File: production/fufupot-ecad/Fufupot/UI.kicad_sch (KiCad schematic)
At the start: 4 parts

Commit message: Updates unfinished
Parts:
- removed BZ1: Buzzer, symbol Device:Buzzer
- removed D1: LED, symbol Device:LED
- removed R1: 220, symbol Device:R
- removed R2: 330, symbol Device:R

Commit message: UI without button
UI schematic without the button
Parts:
- added BZ1: Buzzer, symbol Device:Buzzer
- added D1: LED, symbol Device:LED
- added R1: 220, symbol Device:R
- added R2: 330, symbol Device:R
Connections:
- new net: D1.1 (K), R1.2
- new net D1: BZ1.1 (-)
- new net D2: R1.1
- new net D3: R2.1
- new net GND: BZ1.2 (+), D1.2 (A)
- new net LED_SGN: R2.2

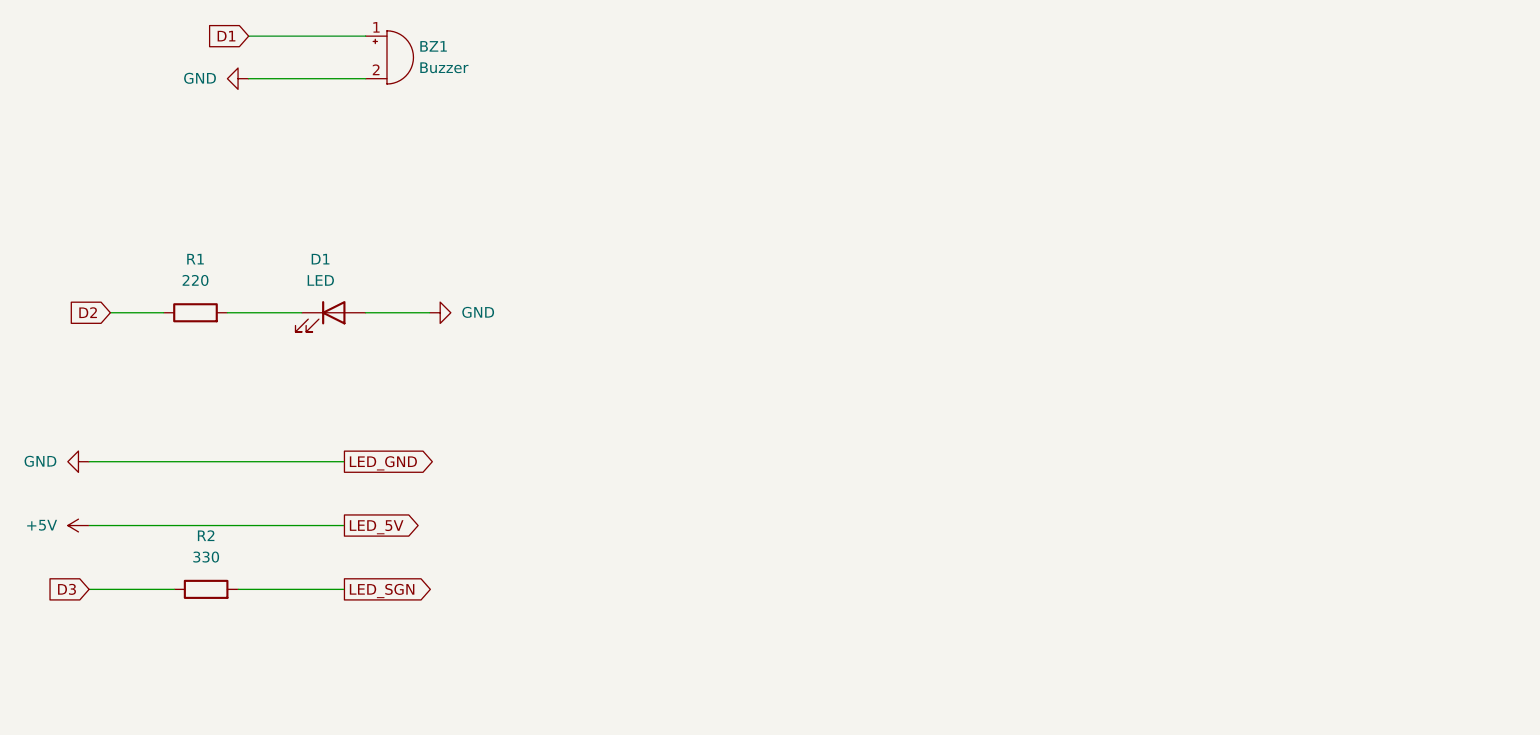
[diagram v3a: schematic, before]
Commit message: UI with Button
Added the button circuit
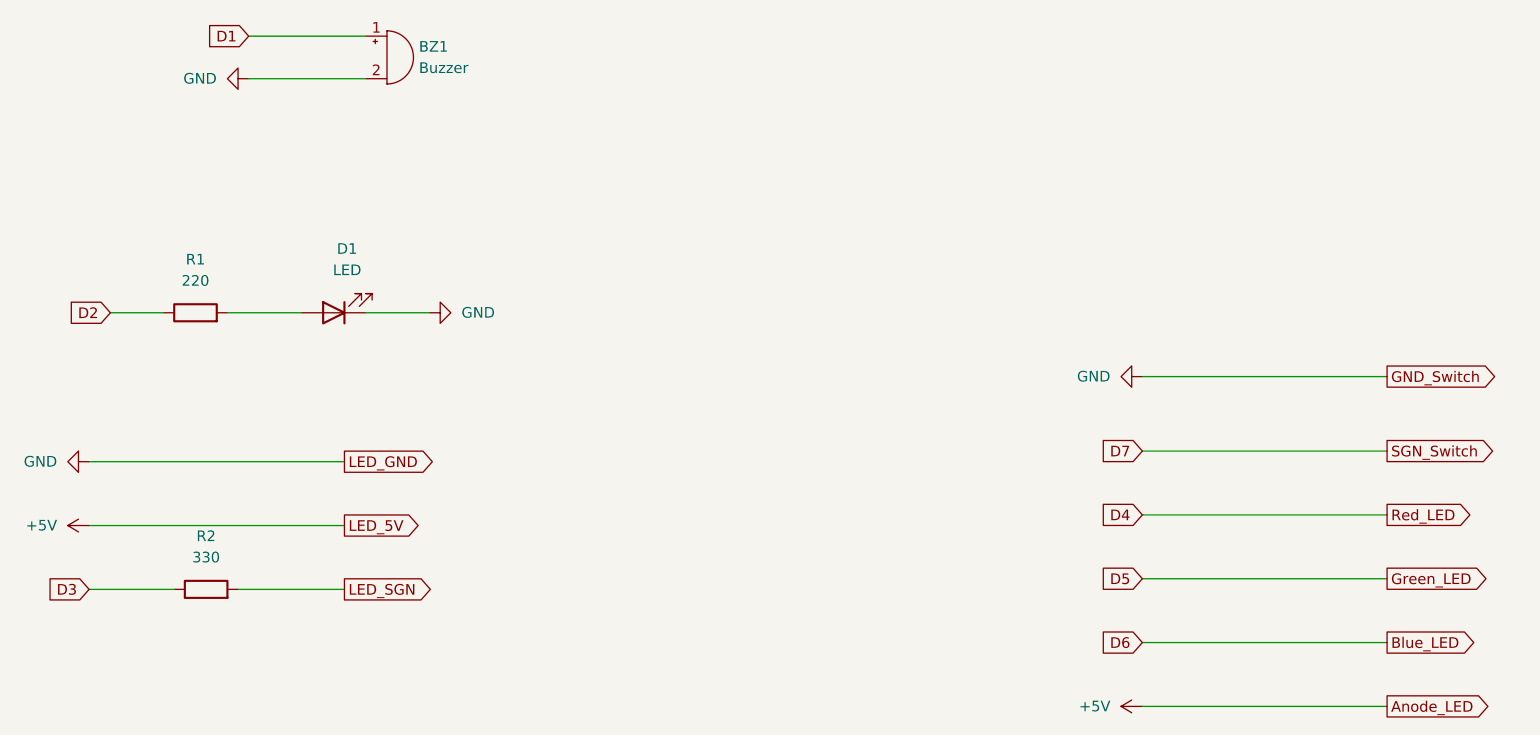
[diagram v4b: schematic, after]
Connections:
- net GND: now also D1.1 (K); no longer D1.2 (A)
- net at R1.2: now also D1.2 (A); no longer D1.1 (K)
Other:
- moved on the sheet: D1
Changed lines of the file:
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@@
 (kicad_sch (version 20230121) (generator eeschema)
   (paper "A4")
+  (wire (pts (xy 165.1 101.6) (xy 194.31 101.6))
+    (stroke (width 0) (type default))
+  )
+  (wire (pts (xy 165.1 124.46) (xy 194.31 124.46))
+    (stroke (width 0) (type default))
+  )
   (wire (pts (xy 58.42 44.45) (xy 72.39 44.45))
     (stroke (width 0) (type default))
@@
     (stroke (width 0) (type default))
   )
+  (wire (pts (xy 165.1 93.98) (xy 194.31 93.98))
+    (stroke (width 0) (type default))
+  )
   (wire (pts (xy 39.37 95.25) (xy 69.85 95.25))
     (stroke (width 0) (type default))
   )
+  (wire (pts (xy 165.1 85.09) (xy 194.31 85.09))
+    (stroke (width 0) (type default))
+  )
   (wire (pts (xy 58.42 49.53) (xy 72.39 49.53))
     (stroke (width 0) (type default))
@@
     (stroke (width 0) (type default))
   )
+  (wire (pts (xy 165.1 109.22) (xy 194.31 109.22))
+    (stroke (width 0) (type default))
+  )
   (wire (pts (xy 55.88 77.47) (xy 64.77 77.47))
     (stroke (width 0) (type default))
   )
+  (wire (pts (xy 165.1 116.84) (xy 194.31 116.84))
+    (stroke (width 0) (type default))
+  )
   (wire (pts (xy 57.15 110.49) (xy 69.85 110.49))
     (stroke (width 0) (type default))
@@
     )
   )
+  (global_label "Red_LED" (shape output) (at 194.31 101.6 0) (fields_autoplaced)
+    (effects (font (size 1.27 1.27)) (justify left))
+    (property "Intersheetrefs" "${INTERSHEET_REFS}" (at 205.2175 101.6 0)
+      (effects (font (size 1.27 1.27)) (justify left) hide)
+    )
+  )
+  (global_label "D5" (shape input) (at 165.1 109.22 180) (fields_autoplaced)
+    (effects (font (size 1.27 1.27)) (justify right))
+    (property "Intersheetrefs" "${INTERSHEET_REFS}" (at 159.6353 109.22 0)
+      (effects (font (size 1.27 1.27)) (justify right) hide)
+    )
+  )
+  (global_label "D6" (shape input) (at 165.1 116.84 180) (fields_autoplaced)
+    (effects (font (size 1.27 1.27)) (justify right))
+    (property "Intersheetrefs" "${INTERSHEET_REFS}" (at 159.6353 116.84 0)
+      (effects (font (size 1.27 1.27)) (justify right) hide)
+    )
+  )
   (global_label "D3" (shape input) (at 39.37 110.49 180) (fields_autoplaced)
     (effects (font (size 1.27 1.27)) (justify right))
@@
     )
   )
+  (global_label "D7" (shape input) (at 165.1 93.98 180) (fields_autoplaced)
+    (effects (font (size 1.27 1.27)) (justify right))
+    (property "Intersheetrefs" "${INTERSHEET_REFS}" (at 159.6353 93.98 0)
+      (effects (font (size 1.27 1.27)) (justify right) hide)
+    )
+  )
   (global_label "LED_GND" (shape output) (at 69.85 95.25 0) (fields_autoplaced)
     (effects (font (size 1.27 1.27)) (justify left))
@@
     )
   )
+  (global_label "D4" (shape input) (at 165.1 101.6 180) (fields_autoplaced)
+    (effects (font (size 1.27 1.27)) (justify right))
+    (property "Intersheetrefs" "${INTERSHEET_REFS}" (at 159.6353 101.6 0)
+      (effects (font (size 1.27 1.27)) (justify right) hide)
+    )
+  )
   (global_label "LED_SGN" (shape output) (at 69.85 110.49 0) (fields_autoplaced)
     (effects (font (size 1.27 1.27)) (justify left))
@@
     )
   )
+  (global_label "Green_LED" (shape output) (at 194.31 109.22 0) (fields_autoplaced)
+    (effects (font (size 1.27 1.27)) (justify left))
+    (property "Intersheetrefs" "${INTERSHEET_REFS}" (at 207.0923 109.22 0)
+      (effects (font (size 1.27 1.27)) (justify left) hide)
+    )
+  )
+  (global_label "Anode_LED" (shape output) (at 194.31 124.46 0) (fields_autoplaced)
+    (effects (font (size 1.27 1.27)) (justify left))
+    (property "Intersheetrefs" "${INTERSHEET_REFS}" (at 207.3341 124.46 0)
+      (effects (font (size 1.27 1.27)) (justify left) hide)
+    )
+  )
   (global_label "D1" (shape input) (at 58.42 44.45 180) (fields_autoplaced)
     (effects (font (size 1.27 1.27)) (justify right))
     (property "Intersheetrefs" "${INTERSHEET_REFS}" (at 52.9553 44.45 0)
       (effects (font (size 1.27 1.27)) (justify right) hide)
+    )
+  )
+  (global_label "Blue_LED" (shape output) (at 194.31 116.84 0) (fields_autoplaced)
+    (effects (font (size 1.27 1.27)) (justify left))
+    (property "Intersheetrefs" "${INTERSHEET_REFS}" (at 205.8827 116.84 0)
+      (effects (font (size 1.27 1.27)) (justify left) hide)
+    )
+  )
+  (global_label "GND_Switch" (shape output) (at 194.31 85.09 0) (fields_autoplaced)
+    (effects (font (size 1.27 1.27)) (justify left))
+    (property "Intersheetrefs" "${INTERSHEET_REFS}" (at 208.2414 85.09 0)
+      (effects (font (size 1.27 1.27)) (justify left) hide)
+    )
+  )
+  (global_label "SGN_Switch" (shape output) (at 194.31 93.98 0) (fields_autoplaced)
+    (effects (font (size 1.27 1.27)) (justify left))
+    (property "Intersheetrefs" "${INTERSHEET_REFS}" (at 208.1809 93.98 0)
+      (effects (font (size 1.27 1.27)) (justify left) hide)
     )
   )
@@
     )
   )
-  (symbol (lib_id "Device:LED") (at 68.58 77.47 0) (unit 1)
-    (in_bom yes) (on_board yes) (dnp no) (fields_autoplaced)
-    (property "Reference" "D1" (at 66.9925 71.12 0)
+  (symbol (lib_id "power:+5V") (at 165.1 124.46 90) (unit 1)
+    (in_bom yes) (on_board yes) (dnp no) (fields_autoplaced)
+    (property "Reference" "#PWR05" (at 168.91 124.46 0)
+      (effects (font (size 1.27 1.27)) hide)
+    )
+    (property "Value" "+5V" (at 161.29 124.46 90)
+      (effects (font (size 1.27 1.27)) (justify left))
+    )
+    (property "Footprint" "" (at 165.1 124.46 0)
+      (effects (font (size 1.27 1.27)) hide)
+    )
+    (property "Datasheet" "" (at 165.1 124.46 0)
+      (effects (font (size 1.27 1.27)) hide)
+    )
+    (pin "1")
+    (instances
+      (project "UI"
+        (path "/1500fb87-98cb-4de3-ba1f-769b7af6205d"
+          (reference "#PWR05") (unit 1)
+        )
+      )
+    )
+  )
+  (symbol (lib_id "Device:LED") (at 68.58 77.47 180) (unit 1)
+    (in_bom yes) (on_board yes) (dnp no) (fields_autoplaced)
+    (property "Reference" "D1" (at 70.1675 69.85 0)
       (effects (font (size 1.27 1.27)))
     )
-    (property "Value" "LED" (at 66.9925 73.66 0)
+    (property "Value" "LED" (at 70.1675 72.39 0)
       (effects (font (size 1.27 1.27)))
     )
@@
         )
       )
+    )
+  )
+  (symbol (lib_id "power:GND") (at 165.1 85.09 270) (unit 1)
+    (in_bom yes) (on_board yes) (dnp no) (fields_autoplaced)
+    (property "Reference" "#PWR06" (at 158.75 85.09 0)
+      (effects (font (size 1.27 1.27)) hide)
+    )
+    (property "Value" "GND" (at 161.29 85.09 90)
+      (effects (font (size 1.27 1.27)) (justify right))
+    )
+    (property "Footprint" "" (at 165.1 85.09 0)
+      (effects (font (size 1.27 1.27)) hide)
+    )
+    (property "Datasheet" "" (at 165.1 85.09 0)
+      (effects (font (size 1.27 1.27)) hide)
+    )
+    (pin "1")
+    (instances
+      (project "UI"
+        (path "/1500fb87-98cb-4de3-ba1f-769b7af6205d"
+          (reference "#PWR06") (unit 1)
+        )
+      )
